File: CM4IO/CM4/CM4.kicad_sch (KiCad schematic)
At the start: 0 parts

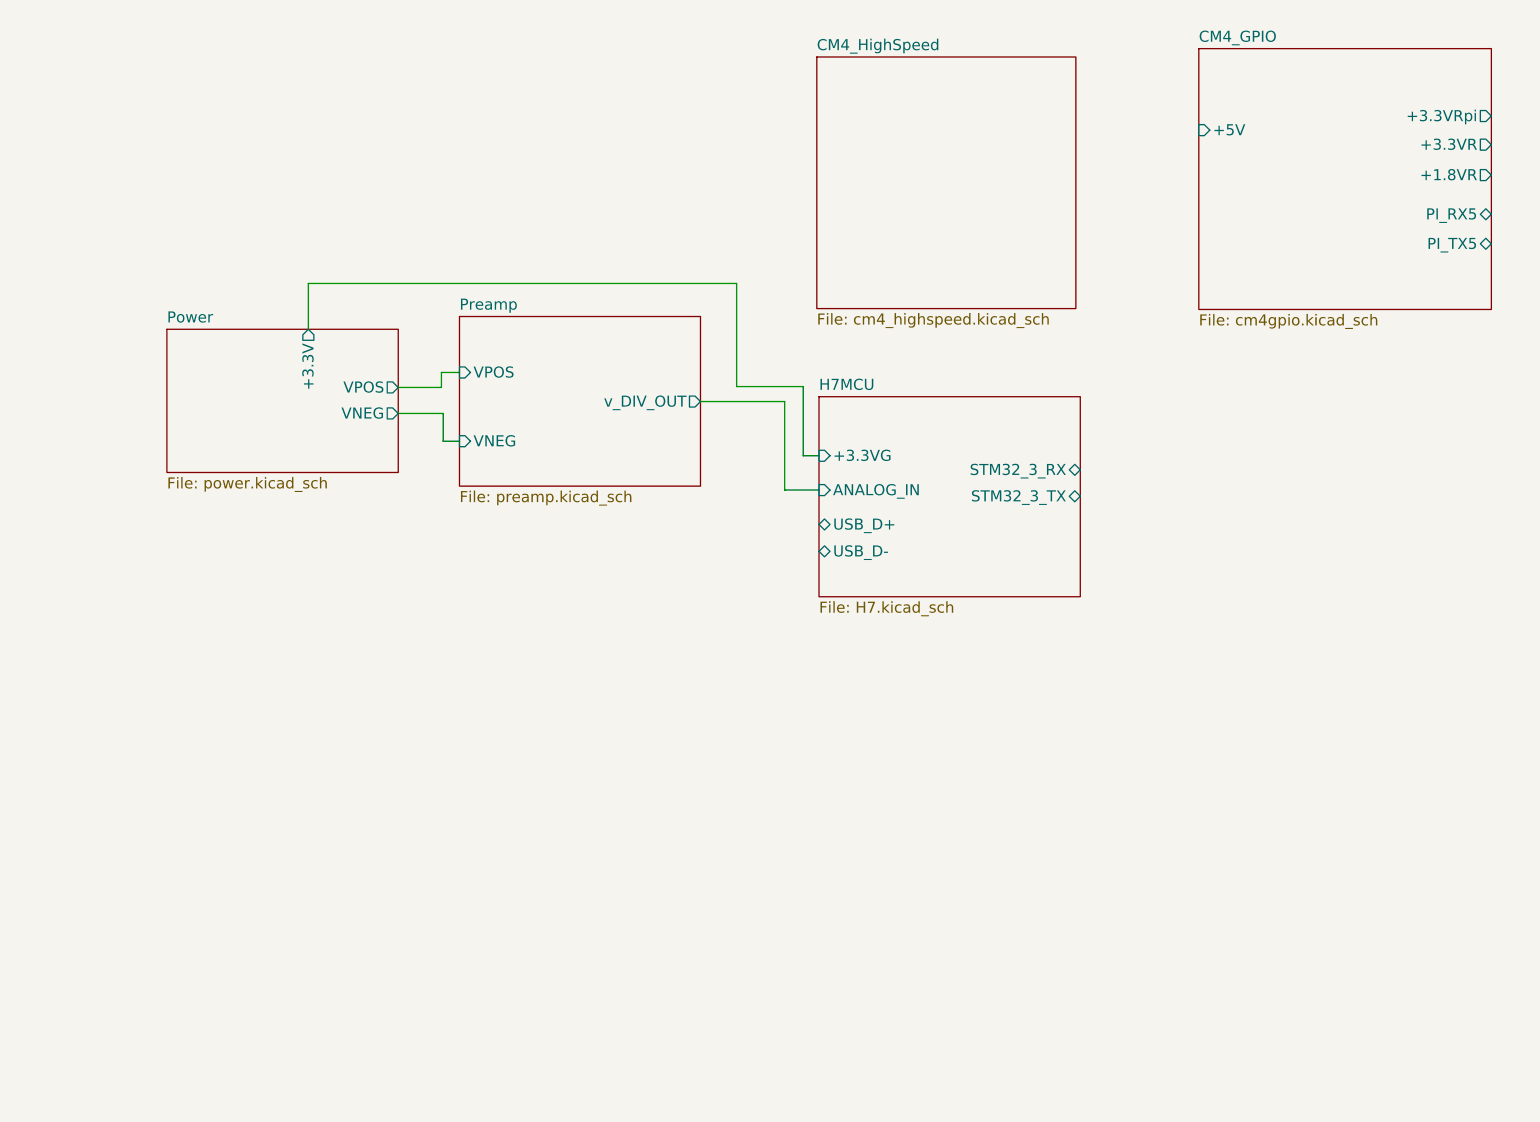
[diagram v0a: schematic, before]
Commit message: Initial CM4IO board design
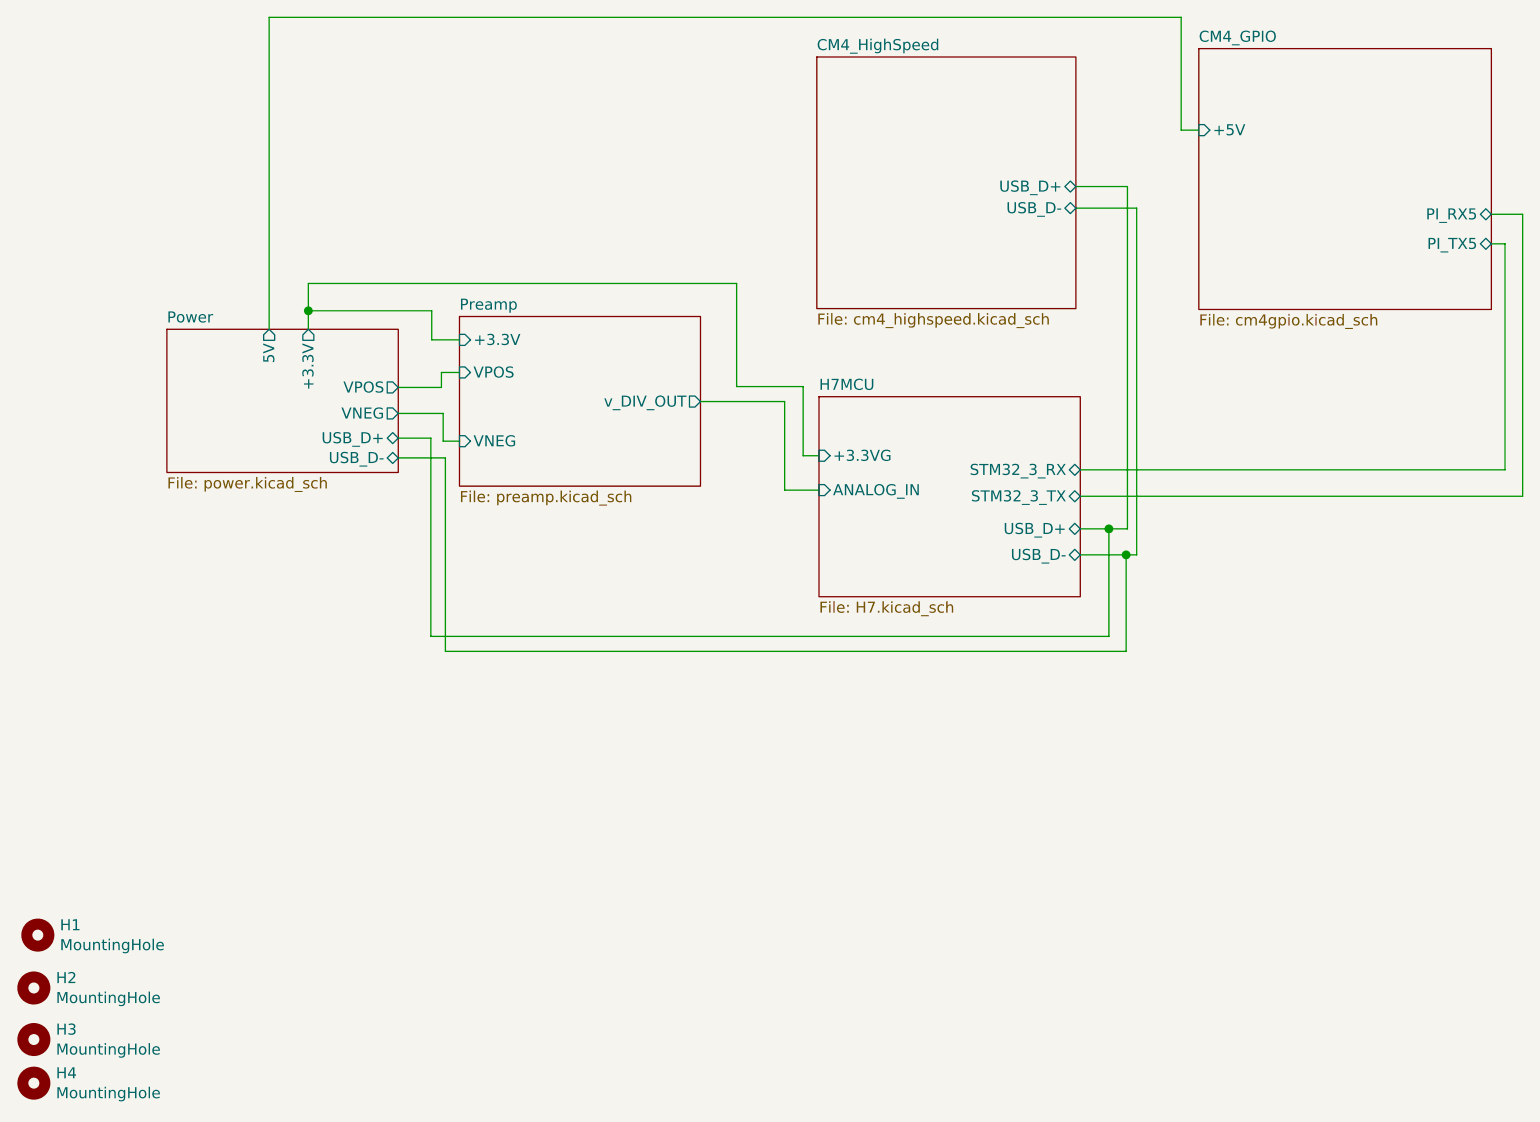
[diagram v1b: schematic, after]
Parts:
- added H1, H2, H3, H4: MountingHole, MountingHole:MountingHole_3.2mm_M3_ISO14580_Pad, symbol Mechanical:MountingHole
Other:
- sheet CM4_GPIO ports: added none; removed +1.8VR, +3.3VR, +3.3VRpi
- sheet CM4_HighSpeed ports: added USB_D+, USB_D-; removed none
- sheet Power ports: added 5V, USB_D+, USB_D-; removed none
- sheet Preamp ports: added +3.3V; removed none
- title: (none) -> PorpDAQ Board - Top Level

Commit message: Completed H7/CM4IO Board
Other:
- sheet Power ports: added none; removed USB_D+, USB_D-
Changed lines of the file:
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@@
   )
   (junction (at 59.944 76.9112) (diameter 1.016) (color 0 0 0 0))
-  (junction (at 152.2476 102.0572) (diameter 1.016) (color 0 0 0 0))
-  (junction (at 154.2288 105.0544) (diameter 1.016) (color 0 0 0 0))
   (wire (pts (xy 55.4228 43.0784) (xy 160.5788 43.0784))
     (stroke (width 0) (type solid) (color 0 0 0 0))
@@
     (stroke (width 0) (type solid) (color 0 0 0 0))
   )
-  (wire (pts (xy 70.3072 91.5924) (xy 74.0664 91.5924))
-    (stroke (width 0) (type solid) (color 0 0 0 0))
-  )
-  (wire (pts (xy 70.3072 93.8784) (xy 75.7428 93.8784))
-    (stroke (width 0) (type solid) (color 0 0 0 0))
-  )
-  (wire (pts (xy 74.0664 91.5924) (xy 74.0664 114.4524))
-    (stroke (width 0) (type solid) (color 0 0 0 0))
-  )
-  (wire (pts (xy 74.0664 114.4524) (xy 152.2476 114.4524))
-    (stroke (width 0) (type solid) (color 0 0 0 0))
-  )
   (wire (pts (xy 74.168 76.9112) (xy 59.944 76.9112))
     (stroke (width 0) (type solid) (color 0 0 0 0))
@@
     (stroke (width 0) (type solid) (color 0 0 0 0))
   )
-  (wire (pts (xy 75.7428 93.8784) (xy 75.7428 116.1796))
-    (stroke (width 0) (type solid) (color 0 0 0 0))
-  )
-  (wire (pts (xy 75.7428 116.1796) (xy 154.2288 116.1796))
-    (stroke (width 0) (type solid) (color 0 0 0 0))
-  )
   (wire (pts (xy 77.3684 80.264) (xy 74.168 80.264))
     (stroke (width 0) (type solid) (color 0 0 0 0))
@@
     (stroke (width 0) (type solid) (color 0 0 0 0))
   )
-  (wire (pts (xy 148.9456 105.0544) (xy 154.2288 105.0544))
-    (stroke (width 0) (type solid) (color 0 0 0 0))
-  )
-  (wire (pts (xy 152.2476 102.0572) (xy 148.9456 102.0572))
-    (stroke (width 0) (type solid) (color 0 0 0 0))
-  )
-  (wire (pts (xy 152.2476 114.4524) (xy 152.2476 102.0572))
-    (stroke (width 0) (type solid) (color 0 0 0 0))
-  )
-  (wire (pts (xy 154.2288 105.0544) (xy 155.448 105.0544))
-    (stroke (width 0) (type solid) (color 0 0 0 0))
-  )
-  (wire (pts (xy 154.2288 116.1796) (xy 154.2288 105.0544))
+  (wire (pts (xy 148.9456 102.0572) (xy 154.3812 102.0572))
+    (stroke (width 0) (type solid) (color 0 0 0 0))
+  )
+  (wire (pts (xy 148.9456 105.0544) (xy 155.448 105.0544))
     (stroke (width 0) (type solid) (color 0 0 0 0))
   )
   (wire (pts (xy 154.3812 62.5856) (xy 154.3812 102.0572))
-    (stroke (width 0) (type solid) (color 0 0 0 0))
-  )
-  (wire (pts (xy 154.3812 102.0572) (xy 152.2476 102.0572))
     (stroke (width 0) (type solid) (color 0 0 0 0))
   )
@@
       (effects (font (size 1.27 1.27)) (justify right))
     )
-    (pin "USB_D+" bidirectional (at 70.3072 91.5924 0)
-      (effects (font (size 1.27 1.27)) (justify right))
-    )
-    (pin "USB_D-" bidirectional (at 70.3072 93.8784 0)
-      (effects (font (size 1.27 1.27)) (justify right))
-    )
     (pin "5V" output (at 55.4228 79.0448 90)
       (effects (font (size 1.27 1.27)) (justify right))
@@
       (reference "#PWR03") (unit 1) (value "VCC") (footprint "")
     )
-    (path "/459be312-3689-4746-960b-38b53c51f6ab/77960939-5528-472f-8d5f-6588d22f7d0c"
-      (reference "#PWR04") (unit 1) (value "GND") (footprint "")
-    )
     (path "/459be312-3689-4746-960b-38b53c51f6ab/329e0bdd-b54a-45ca-96f7-6adb6b0ea95b"
       (reference "#PWR05") (unit 1) (value "GND") (footprint "")
@@
       (reference "R28") (unit 1) (value "2.2k") (footprint "Resistor_SMD:R_0603_1608Metric")
     )
-    (path "/459be312-3689-4746-960b-38b53c51f6ab/d5f5b805-dfa2-4f0f-9bc9-af4f5358e95d"
-      (reference "U1") (unit 1) (value "USBLC6-2SC6") (footprint "Package_TO_SOT_SMD:SOT-23-6")
+    (path "/7d743eaf-baa5-43f2-8d69-669f9701f418/8992e62f-11a6-4957-9f45-bc6fd5c7953f"
+      (reference "#PWR04") (unit 1) (value "GND") (footprint "")
     )
     (path "/7d743eaf-baa5-43f2-8d69-669f9701f418/43b4bed3-7448-4671-971e-045ff47edc51"
@@
       (reference "IC3") (unit 1) (value "LMH6643MAX_NOPB") (footprint "SamacSys_Parts:SOIC127P600X175-8N")
     )
-    (path "/7d743eaf-baa5-43f2-8d69-669f9701f418/00d884b9-7832-4732-b051-875e7a51542b"
-      (reference "J1") (unit 1) (value "901-144-8RFX") (footprint "9011448RFX")
+    (path "/7d743eaf-baa5-43f2-8d69-669f9701f418/8cedd2fb-2aae-4292-94c1-e3c29b678f94"
+      (reference "J1") (unit 1) (value "Conn_Coaxial") (footprint "Connector_Coaxial:SMA_Samtec_SMA-J-P-H-ST-EM1_EdgeMount")
+    )
+    (path "/7d743eaf-baa5-43f2-8d69-669f9701f418/7ccf9aed-fc01-4747-829f-b2699cf5e207"
+      (reference "J6") (unit 1) (value "Conn_01x02_Female") (footprint "Connector_PinHeader_2.54mm:PinHeader_1x02_P2.54mm_Horizontal")
     )
     (path "/7d743eaf-baa5-43f2-8d69-669f9701f418/19bd3c4a-12f9-4aa5-a2f0-e700ed369ab6"
@@
       (reference "D2") (unit 1) (value "LED_Red") (footprint "LED_SMD:LED_0603_1608Metric")
     )
+    (path "/9a9f1666-918f-4f2c-af79-4cac717b768c/f20690d7-ea35-42bc-bc13-eada977dc558"
+      (reference "FB2") (unit 1) (value "100 @ 100 MHz") (footprint "Inductor_SMD:L_0603_1608Metric")
+    )
     (path "/9a9f1666-918f-4f2c-af79-4cac717b768c/89774ec3-d57d-4830-aa14-5b164b2f90b2"
       (reference "FB3") (unit 1) (value "18 @100Mhz") (footprint "Inductor_SMD:L_0603_1608Metric")
@@
       (reference "L4") (unit 1) (value "2.2uH") (footprint "Inductor_SMD:L_0805_2012Metric")
     )
-    (path "/9a9f1666-918f-4f2c-af79-4cac717b768c/095c03a1-2661-4bbf-a680-779d2ea9138a"
-      (reference "L5") (unit 1) (value "39n") (footprint "Inductor_SMD:L_0402_1005Metric")
-    )
     (path "/9a9f1666-918f-4f2c-af79-4cac717b768c/d8465388-ac22-48f4-b9ae-096aa3087a58"
-      (reference "R18") (unit 1) (value "0") (footprint "Resistor_SMD:R_0402_1005Metric")
+      (reference "R18") (unit 1) (value "47") (footprint "Resistor_SMD:R_0402_1005Metric")
     )
     (path "/9a9f1666-918f-4f2c-af79-4cac717b768c/84c8e622-8cd5-4d34-be56-9c59cad97af8"
@@
       (reference "S1") (unit 1) (value "TL1105CF160Q") (footprint "SamacSys_Parts:TL1105CF160Q")
     )
-    (path "/9a9f1666-918f-4f2c-af79-4cac717b768c/0dcce734-8291-4c13-a677-155f14178197"
-      (reference "SW1") (unit 1) (value "SW_SPDT") (footprint "Button_Switch_SMD:SW_SPDT_PCM12")
-    )
     (path "/9a9f1666-918f-4f2c-af79-4cac717b768c/1851d148-7b56-4a22-b7f5-8db303f52234"
